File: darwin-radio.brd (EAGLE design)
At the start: 110 x 72.9 mm, 40 parts, among them Q2 NDS8434, U1 ATWINC, U6 MCP7384X

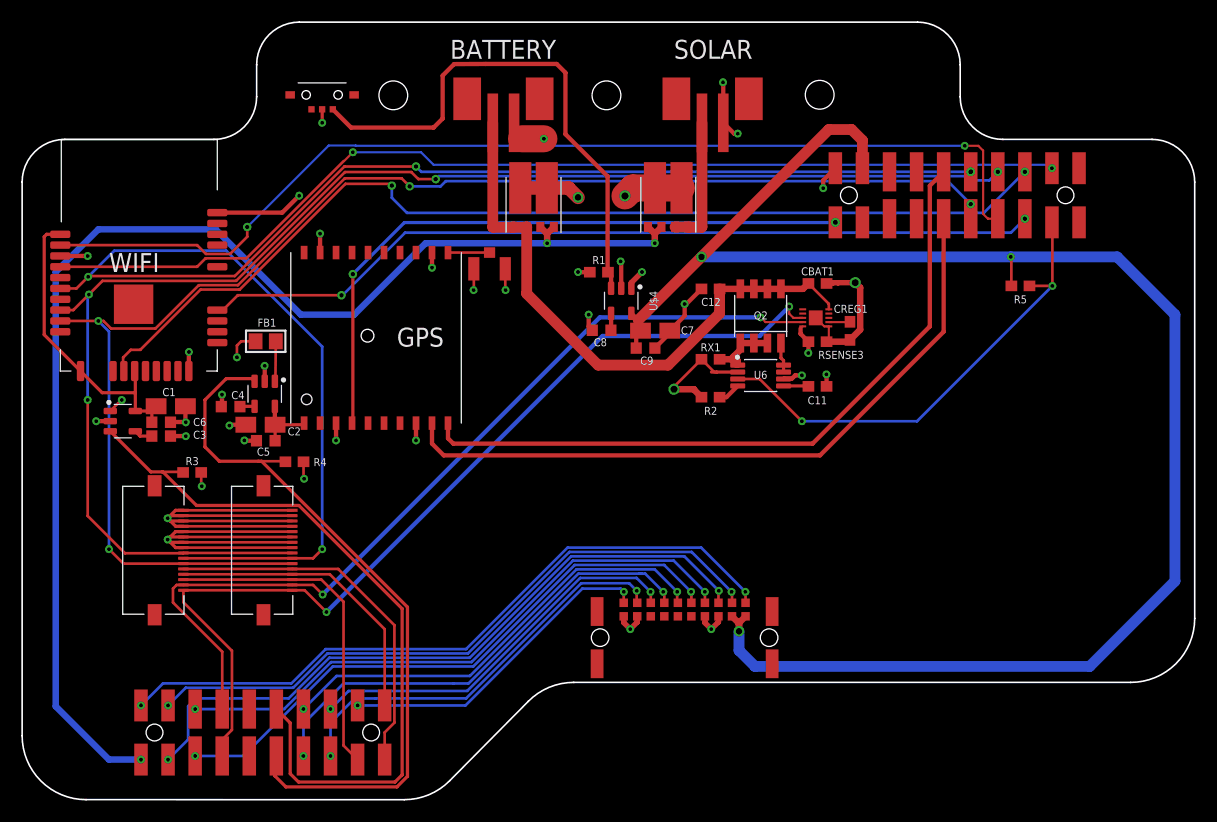
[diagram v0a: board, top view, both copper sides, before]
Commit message: Fixed Wifi enable, Radio Pullups, BAT+ connection on charger, and internal layer shorts to various vias.
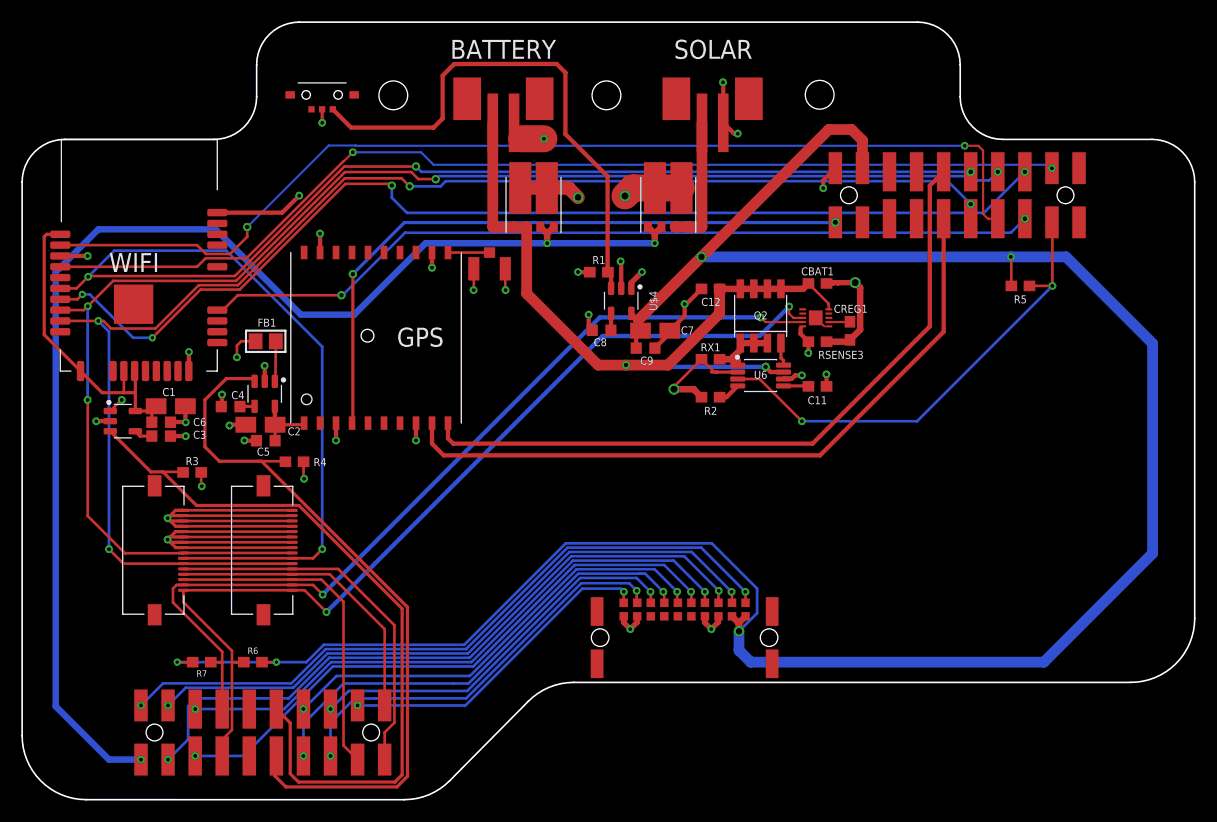
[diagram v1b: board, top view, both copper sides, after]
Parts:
- added R6, R7: 100k, SparkFun-Resistors:0603
- renumbered U$10 to J3, U$8 to J1, U$9 to J2
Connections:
- net 3V3: now also R6.2, R7.2
- net BAT+: now also U6.7
- net N$17: no longer U6.7
- net RAD_SCL: now also R6.1
- net RAD_SDA: now also R7.1
- net WIFI_3V3: now also U1.22
- net WIFI_CS: now also U1.16; no longer U1.22
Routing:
- net UNREG: track 525.2 -> 65.5 mm
- net GND: track 458.1 -> 125.3 mm
- net 3V3: track 159.6 -> 220.3 mm, vias 3 -> 5
- net BAT+: track 56.5 -> 71.5 mm, vias 0 -> 2
- net WIFI_CS: track 96.0 -> 101.7 mm, vias 2 -> 4
- net WIFI_3V3: track 28.6 -> 30.6 mm
- net BAT-: track 50.7 -> 49.1 mm
- net RADIO_MISO: track 135.7 -> 134.5 mm
- net RAD_SCL: track 89.5 -> 90.6 mm
- net RAD_SDA: track 83.8 -> 84.8 mm
- net N$17: track 2.82 -> 2.17 mm
